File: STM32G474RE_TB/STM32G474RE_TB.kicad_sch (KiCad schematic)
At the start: 14 parts, among them U1 STM32G474RETx, U10 L7805, U2 XC6206P332MR-G, U3 REF3125

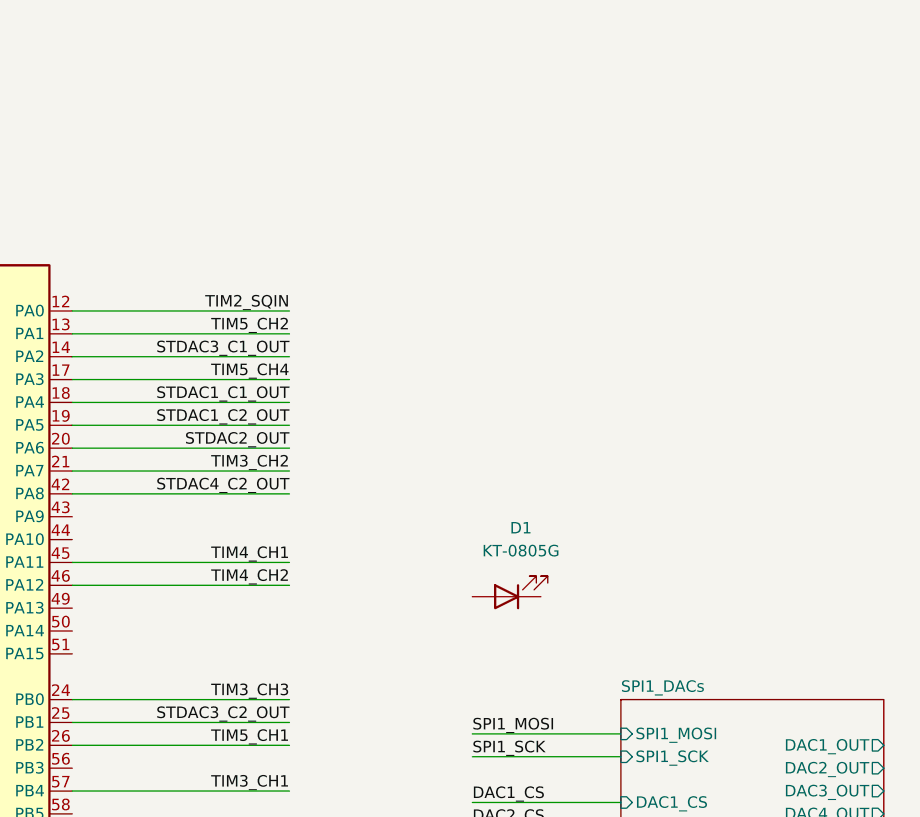
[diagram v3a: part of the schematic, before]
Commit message: Adjusted layouts and added DAC buffer from stm32.
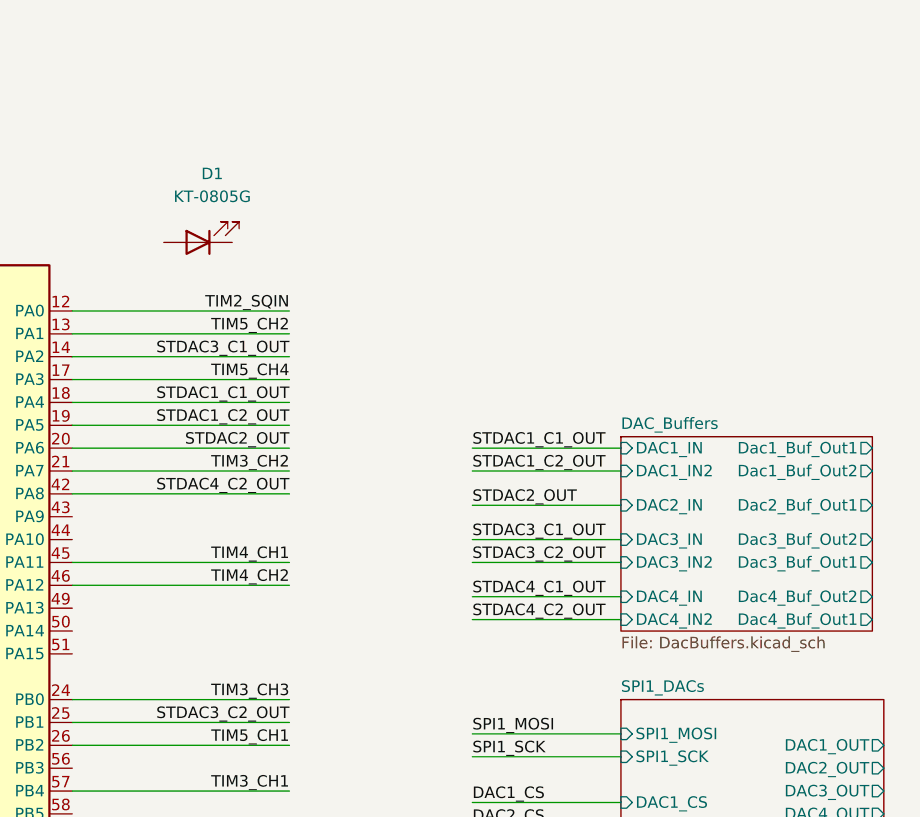
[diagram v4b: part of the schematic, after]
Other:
- added sheet DAC_Buffers (DacBuffers.kicad_sch)
- moved on the sheet: D1

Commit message: Added MOSFET template with led for debug or other functions
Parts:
- removed D1: KT-0805G, LED_SMD:LED_0805_2012Metric, symbol Device:LED
- renumbered C21 to C6, C22 to C7, C6 to C8, C7 to C9, U10 to U2, U2 to U3, U3 to U4
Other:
- added sheet LED's and FET's (TIM_LED_FET.kicad_sch)
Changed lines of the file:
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@@
 		(dnp no)
 		(fields_autoplaced yes)
-		(property "Reference" "C22"
+		(property "Reference" "C7"
 			(at 82.55 173.9899 0)
 			(effects
@@
 			(project "STM32G474RE_TB"
 				(path "/c8ed293a-fe87-496b-9ed5-e9e5575d3b65"
-					(reference "C22")
+					(reference "C7")
 					(unit 1)
 				)
@@
 		(dnp no)
 		(fields_autoplaced yes)
-		(property "Reference" "U3"
+		(property "Reference" "U4"
 			(at 143.51 176.5299 0)
 			(effects
@@
 			(project "STM32G474RE_TB"
 				(path "/c8ed293a-fe87-496b-9ed5-e9e5575d3b65"
-					(reference "U3")
+					(reference "U4")
 					(unit 1)
 				)
@@
 	)
 	(symbol
-		(lib_id "Device:LED")
-		(at 163.83 43.18 180)
-		(unit 1)
-		(exclude_from_sim no)
-		(in_bom yes)
-		(on_board yes)
-		(dnp no)
-		(fields_autoplaced yes)
-		(property "Reference" "D1"
-			(at 165.4175 35.56 0)
-			(effects
-				(font
-					(size 1.27 1.27)
-				)
-			)
-		)
-		(property "Value" "KT-0805G"
-			(at 165.4175 38.1 0)
-			(effects
-				(font
-					(size 1.27 1.27)
-				)
-			)
-		)
-		(property "Footprint" "LED_SMD:LED_0805_2012Metric"
-			(at 163.83 43.18 0)
-			(effects
-				(font
-					(size 1.27 1.27)
-				)
-				(hide yes)
-			)
-		)
-		(property "Datasheet" "~"
-			(at 163.83 43.18 0)
-			(effects
-				(font
-					(size 1.27 1.27)
-				)
-				(hide yes)
-			)
-		)
-		(property "Description" "Light emitting diode"
-			(at 163.83 43.18 0)
-			(effects
-				(font
-					(size 1.27 1.27)
-				)
-				(hide yes)
-			)
-		)
-		(property "Sim.Pins" "1=K 2=A"
-			(at 163.83 43.18 0)
-			(effects
-				(font
-					(size 1.27 1.27)
-				)
-				(hide yes)
-			)
-		)
-		(pin "1"
-		)
-		(pin "2"
-		)
-		(instances
-			(project ""
-				(path "/c8ed293a-fe87-496b-9ed5-e9e5575d3b65"
-					(reference "D1")
-					(unit 1)
-				)
-			)
-		)
-	)
-	(symbol
 		(lib_id "power:GND")
 		(at 154.94 165.1 0)
@@
 		(dnp no)
 		(fields_autoplaced yes)
-		(property "Reference" "#PWR046"
+		(property "Reference" "#PWR012"
 			(at 66.04 187.96 0)
 			(effects
@@
 			(project "STM32G474RE_TB"
 				(path "/c8ed293a-fe87-496b-9ed5-e9e5575d3b65"
-					(reference "#PWR046")
+					(reference "#PWR012")
 					(unit 1)
 				)
@@
 		(dnp no)
 		(fields_autoplaced yes)
-		(property "Reference" "#PWR013"
+		(property "Reference" "#PWR016"
 			(at 147.32 193.04 0)
 			(effects
@@
 			(project "STM32G474RE_TB"
 				(path "/c8ed293a-fe87-496b-9ed5-e9e5575d3b65"
-					(reference "#PWR013")
+					(reference "#PWR016")
 					(unit 1)
 				)
@@
 		(dnp no)
 		(fields_autoplaced yes)
-		(property "Reference" "#PWR048"
+		(property "Reference" "#PWR07"
 			(at 49.53 175.26 0)
 			(effects
@@
 			(project ""
 				(path "/c8ed293a-fe87-496b-9ed5-e9e5575d3b65"
-					(reference "#PWR048")
+					(reference "#PWR07")
 					(unit 1)
 				)
@@
 		(dnp no)
 		(fields_autoplaced yes)
-		(property "Reference" "#PWR09"
+		(property "Reference" "#PWR011"
 			(at 162.56 181.61 0)
 			(effects
@@
 			(project "STM32G474RE_TB"
 				(path "/c8ed293a-fe87-496b-9ed5-e9e5575d3b65"
-					(reference "#PWR09")
+					(reference "#PWR011")
 					(unit 1)
 				)
@@
 		(dnp no)
 		(fields_autoplaced yes)
-		(property "Reference" "U2"
+		(property "Reference" "U3"
 			(at 110.49 167.64 0)
 			(effects
@@
 			(project ""
 				(path "/c8ed293a-fe87-496b-9ed5-e9e5575d3b65"
-					(reference "U2")
+					(reference "U3")
 					(unit 1)
 				)
@@
 		(dnp no)
 		(fields_autoplaced yes)
-		(property "Reference" "U10"
+		(property "Reference" "U2"
 			(at 66.04 165.1 0)
 			(effects
@@
 			(project ""
 				(path "/c8ed293a-fe87-496b-9ed5-e9e5575d3b65"
-					(reference "U10")
+					(reference "U2")
 					(unit 1)
 				)
@@
 		(dnp no)
 		(fields_autoplaced yes)
-		(property "Reference" "#PWR07"
+		(property "Reference" "#PWR09"
 			(at 93.98 176.53 0)
 			(effects
@@
 			(project "STM32G474RE_TB"
 				(path "/c8ed293a-fe87-496b-9ed5-e9e5575d3b65"
-					(reference "#PWR07")
+					(reference "#PWR09")
 					(unit 1)
 				)
@@
 		(dnp no)
 		(fields_autoplaced yes)
-		(property "Reference" "#PWR010"
+		(property "Reference" "#PWR013"
 			(at 93.98 187.96 0)
 			(effects
@@
 			(project "STM32G474RE_TB"
 				(path "/c8ed293a-fe87-496b-9ed5-e9e5575d3b65"
-					(reference "#PWR010")
+					(reference "#PWR013")
 					(unit 1)
 				)
@@
 		(dnp no)
 		(fields_autoplaced yes)
-		(property "Reference" "#PWR012"
+		(property "Reference" "#PWR015"
 			(at 123.19 187.96 0)
 			(effects
@@
 			(project "STM32G474RE_TB"
 				(path "/c8ed293a-fe87-496b-9ed5-e9e5575d3b65"
-					(reference "#PWR012")
+					(reference "#PWR015")
 					(unit 1)
 				)
@@
 		(dnp no)
 		(fields_autoplaced yes)
-		(property "Reference" "C21"
+		(property "Reference" "C6"
 			(at 53.34 173.9899 0)
 			(effects
@@
 			(project "STM32G474RE_TB"
 				(path "/c8ed293a-fe87-496b-9ed5-e9e5575d3b65"
-					(reference "C21")
+					(reference "C6")
 					(unit 1)
 				)
@@
 		(dnp no)
 		(fields_autoplaced yes)
-		(property "Reference" "C6"
+		(property "Reference" "C8"
 			(at 97.79 176.5299 0)
 			(effects
@@
 			(project "STM32G474RE_TB"
 				(path "/c8ed293a-fe87-496b-9ed5-e9e5575d3b65"
-					(reference "C6")
+					(reference "C8")
 					(unit 1)
 				)
@@
 		(dnp no)
 		(fields_autoplaced yes)
-		(property "Reference" "#PWR08"
+		(property "Reference" "#PWR010"
 			(at 123.19 177.8 0)
 			(effects
@@
 			(project "STM32G474RE_TB"
 				(path "/c8ed293a-fe87-496b-9ed5-e9e5575d3b65"
-					(reference "#PWR08")
+					(reference "#PWR010")
 					(unit 1)
 				)
@@
 		(dnp no)
 		(fields_autoplaced yes)
-		(property "Reference" "#PWR011"
+		(property "Reference" "#PWR014"
 			(at 110.49 187.96 0)
 			(effects
@@
 			(project "STM32G474RE_TB"
 				(path "/c8ed293a-fe87-496b-9ed5-e9e5575d3b65"
-					(reference "#PWR011")
+					(reference "#PWR014")
 					(unit 1)
 				)
@@
 		(dnp no)
 		(fields_autoplaced yes)
-		(property "Reference" "#PWR047"
+		(property "Reference" "#PWR08"
 			(at 78.74 175.26 0)
 			(effects
@@
 			(project "STM32G474RE_TB"
 				(path "/c8ed293a-fe87-496b-9ed5-e9e5575d3b65"
-					(reference "#PWR047")
+					(reference "#PWR08")
 					(unit 1)
 				)
@@
 		(dnp no)
 		(fields_autoplaced yes)
-		(property "Reference" "C7"
+		(property "Reference" "C9"
 			(at 127 176.5299 0)
 			(effects
@@
 			(project "STM32G474RE_TB"
 				(path "/c8ed293a-fe87-496b-9ed5-e9e5575d3b65"
-					(reference "C7")
+					(reference "C9")
 					(unit 1)
 				)
@@
 				)
 			)
+		)
+	)
+	(sheet
+		(at 48.26 119.38)
+		(size 39.37 20.32)
+		(exclude_from_sim no)
+		(in_bom yes)
+		(on_board yes)
+		(dnp no)
+		(fields_autoplaced yes)
+		(stroke
+			(width 0.1524)
+			(type solid)
+		)
+		(fill
+			(color 0 0 0 0.0000)
+		)
+		(property "Sheetname" "LED's and FET's"
+			(at 48.26 118.6684 0)
+			(effects
+				(font
+					(size 1.27 1.27)
+				)
+				(justify left bottom)
+			)
+		)
+		(property "Sheetfile" "TIM_LED_FET.kicad_sch"
+			(at 48.26 140.2846 0)
+			(effects
+				(font
+					(size 1.27 1.27)
+				)
+				(justify left top)
+			)
+		)
+		(instances
+			(project "STM32G474RE_TB"
+				(path "/c8ed293a-fe87-496b-9ed5-e9e5575d3b65"
+					(page "5")
+				)
+			)
